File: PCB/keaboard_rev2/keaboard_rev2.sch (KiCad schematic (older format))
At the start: 78 parts, among them J1 AudioJack4, SW1 SW_Push, SW10 SW_Push, SW11 SW_Push, SW12 SW_Push, SW13 SW_Push, SW14 SW_Push, SW15 SW_Push, SW16 SW_Push, SW17 SW_Push, SW18 SW_Push, SW19 SW_Push, SW2 SW_Push, SW20 SW_Push, SW21 SW_Push, SW22 SW_Push, SW23 SW_Push, SW24 SW_Push, SW25 SW_Push, SW3 SW_Push, SW4 SW_Push, SW5 SW_Push, SW6 SW_Push, SW7 SW_Push, SW8 SW_Push, SW9 SW_Push, U1 ProMicro

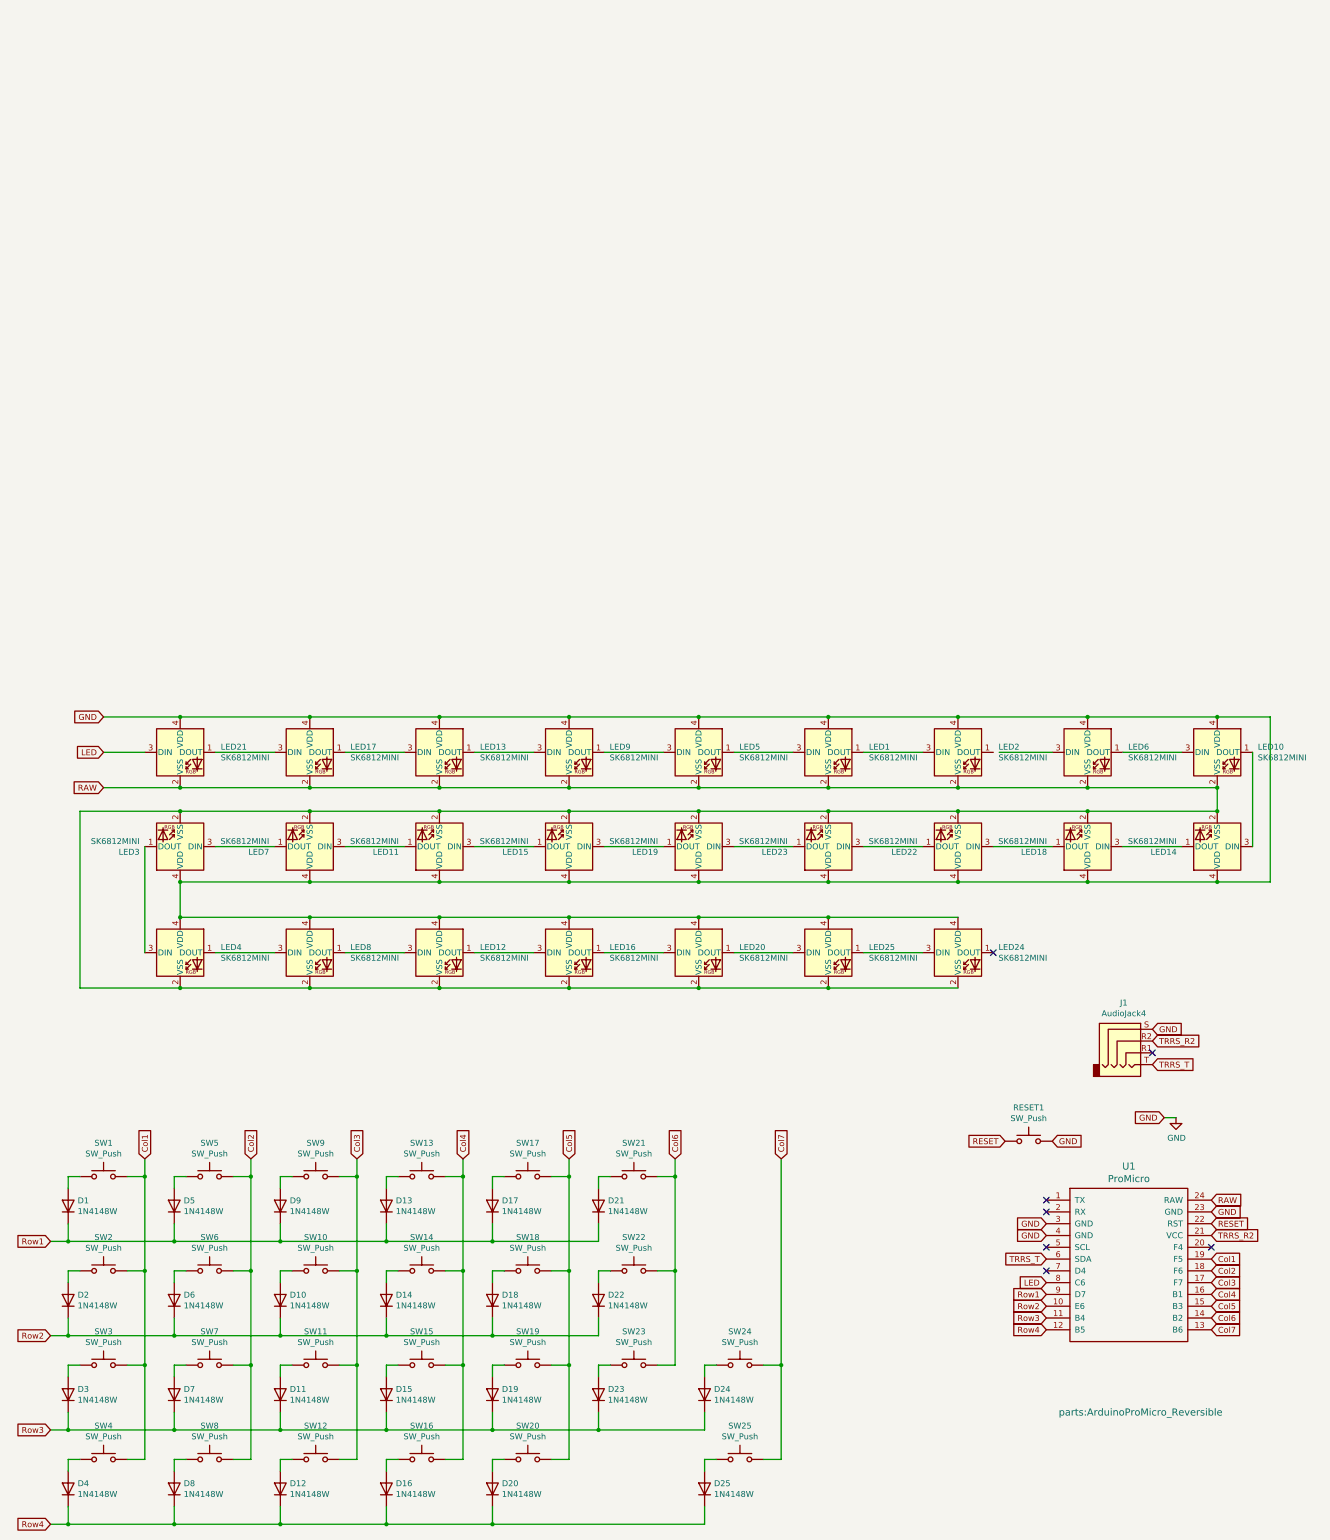
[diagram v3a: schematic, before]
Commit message: Better footprints, OLED, misc
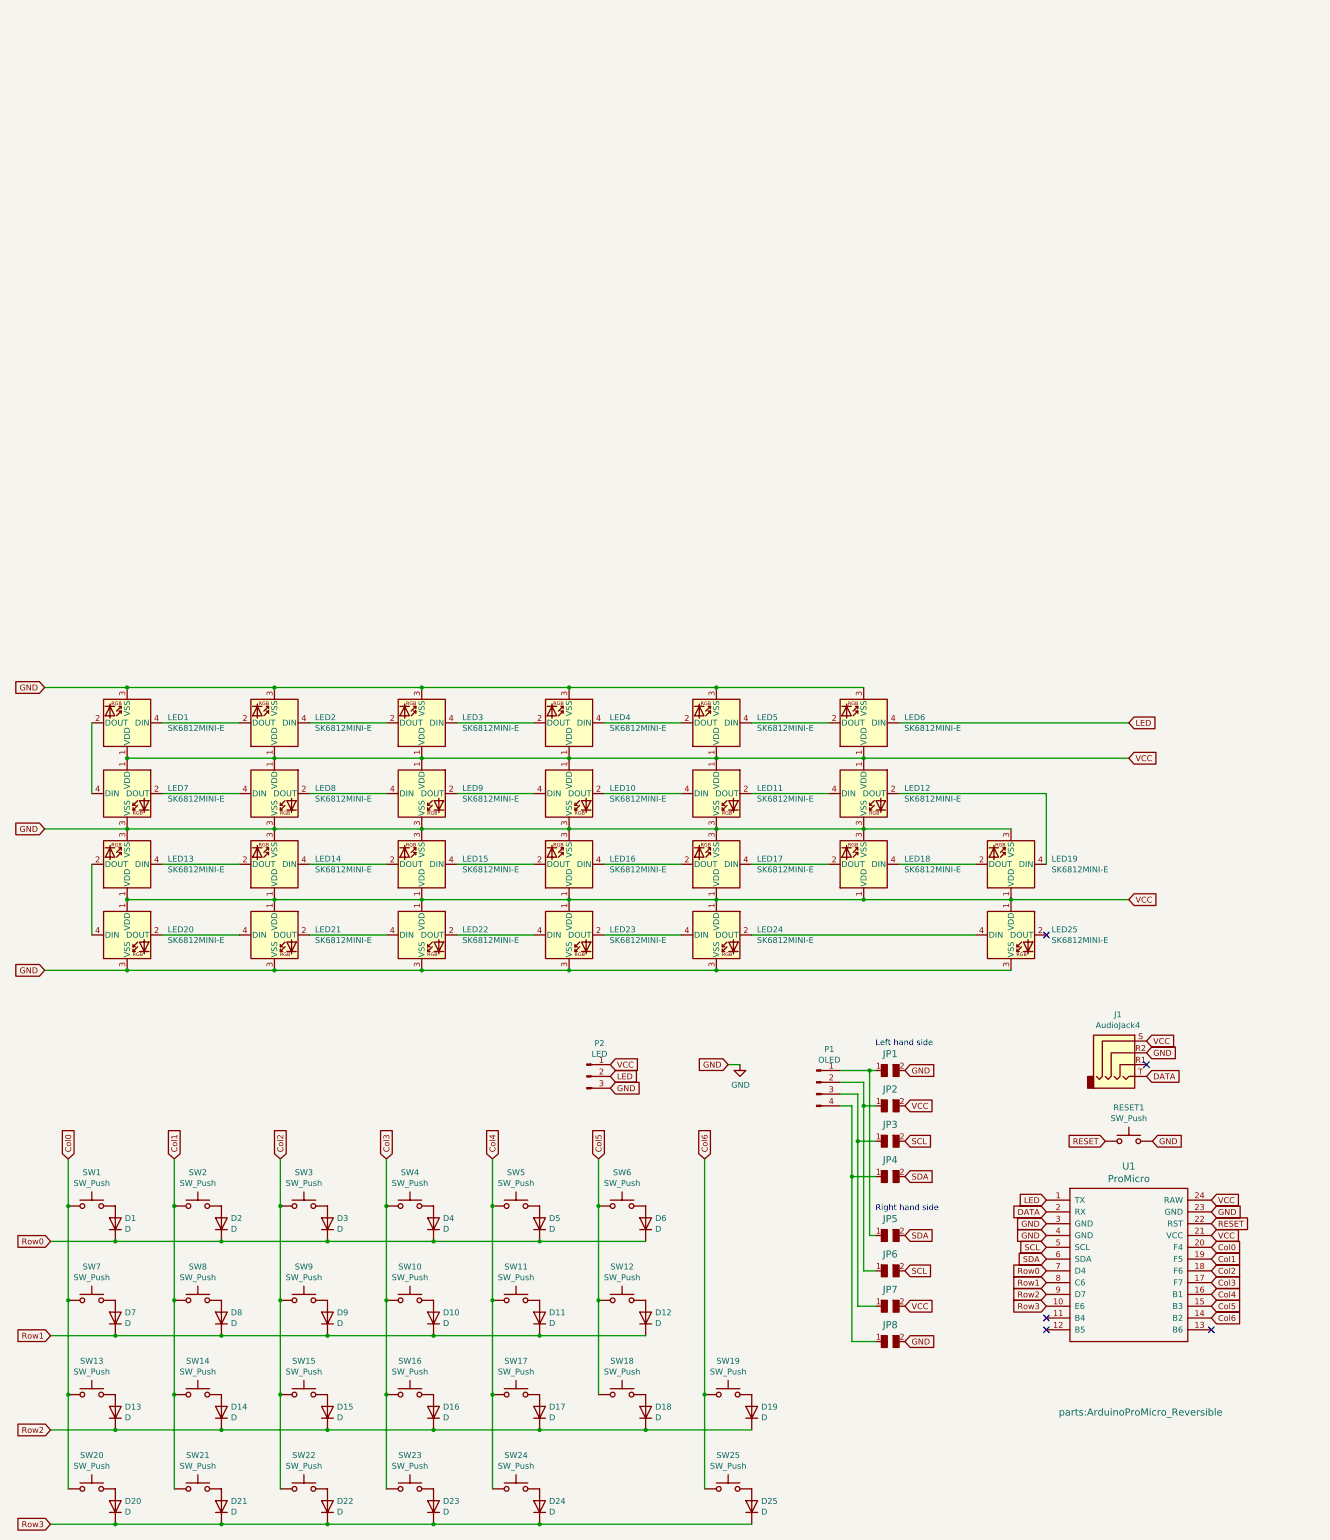
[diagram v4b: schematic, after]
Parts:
- removed LED1, LED10, LED11, LED12, LED13, LED14, LED15, LED16, LED17, LED18, LED19, LED2, LED20, LED21, LED22, LED23, LED24, LED25, LED3, LED4, LED5, LED6, LED7, LED8, LED9: SK6812MINI, parts:YS-SK6812MINI-E_reversible, symbol LED:SK6812MINI
- added JP1, JP8: GND, kbd:Jumper, symbol keyboard_parts:SOLDER_JUMPER
- added JP2, JP7: VCC, kbd:Jumper, symbol keyboard_parts:SOLDER_JUMPER
- added JP3, JP6: SCL, kbd:Jumper, symbol keyboard_parts:SOLDER_JUMPER
- added JP4, JP5: SDA, kbd:Jumper, symbol keyboard_parts:SOLDER_JUMPER
- added LED1, LED10, LED11, LED12, LED13, LED14, LED15, LED16, LED17, LED18, LED19, LED2, LED20, LED21, LED22, LED23, LED24, LED25, LED3, LED4, LED5, LED6, LED7, LED8, LED9: SK6812MINI-E, parts:SK6812MINI-E_reversible, symbol kicad-keyboard-parts:SK6812MINI-E
- added P1: OLED, kbd:OLED_v2, symbol Connector:Conn_01x04_Male
- added P2: LED, parts:StripLED_reversible, symbol Connector:Conn_01x03_Male
- D1, D10, D11, D12, D13, D14, D15, D16, D17, D18, D19, D2, D20, D21, D22, D23, D24, D25, D3, D4, D5, D6, D7, D8, D9: value 1N4148W -> D; footprint parts:D_SOD123_reversible -> Keebio-Parts:Diode-dual
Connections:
- net Col1: now also SW14.1, SW2.1, SW21.1, SW8.1; no longer SW1.2, SW2.2, SW3.2, SW4.2
- net Col2: now also SW15.1, SW22.1, SW3.1, SW9.1; no longer SW5.2, SW6.2, SW7.2, SW8.2
- net Col3: now also SW10.1, SW16.1, SW23.1, SW4.1; no longer SW10.2, SW11.2, SW12.2, SW9.2
- net Col4: now also SW11.1, SW17.1, SW24.1, SW5.1; no longer SW13.2, SW14.2, SW15.2, SW16.2
- net Col5: now also SW12.1, SW18.1, SW6.1; no longer SW17.2, SW18.2, SW19.2, SW20.2
- net Col6: now also SW19.1, SW25.1; no longer SW21.2, SW22.2, SW23.2
- net GND: now also J1.R2, JP1.2, JP8.2, LED1.3 (VSS), LED10.3 (VSS), LED11.3 (VSS), LED12.3 (VSS), LED13.3 (VSS), LED14.3 (VSS), LED15.3 (VSS), LED16.3 (VSS), LED17.3 (VSS), LED18.3 (VSS), LED19.3 (VSS), LED2.3 (VSS), LED20.3 (VSS), LED21.3 (VSS), LED22.3 (VSS), LED23.3 (VSS), LED24.3 (VSS), LED25.3 (VSS), LED3.3 (VSS), LED4.3 (VSS), LED5.3 (VSS), LED6.3 (VSS), LED7.3 (VSS), LED8.3 (VSS), LED9.3 (VSS), P2.3 (Pin_3); no longer J1.S
- net LED: now also U1.1 (TX), LED6.4 (DIN), P2.2 (Pin_2); no longer U1.8 (C6)
- net Row1: now also D10.1 (K), D11.1 (K), D12.1 (K), D7.1 (K), D8.1 (K), U1.8 (C6); no longer D1.1 (K), D13.1 (K), D17.1 (K), D21.1 (K), D5.1 (K), U1.9 (D7)
- net Row2: now also D13.1 (K), D15.1 (K), D16.1 (K), D17.1 (K), D19.1 (K), U1.9 (D7); no longer D10.1 (K), D2.1 (K), D22.1 (K), D6.1 (K), U1.10 (E6)
- net Row3: now also D20.1 (K), D21.1 (K), D22.1 (K), D25.1 (K), U1.10 (E6); no longer D11.1 (K), D15.1 (K), D19.1 (K), D3.1 (K), D7.1 (K), U1.11 (B4)
- net DATA: now reaches U1.2 (RX)
- net DATA: now also J1.T
- net Col0: now reaches U1.20 (F4)
- net Col0: now also SW1.1, SW13.1, SW20.1, SW7.1
- net SCL: now reaches U1.5 (SCL)
- net SCL: now also JP3.2, JP6.2
- net Row0: now reaches U1.7 (D4)
- net Row0: now also D1.1 (K), D2.1 (K), D3.1 (K), D4.1 (K), D5.1 (K), D6.1 (K)
- net at D1.2 (A): now also SW1.2; no longer SW1.1
- net at D5.2 (A): now also SW5.2; no longer SW5.1
- net at D9.2 (A): now also SW9.2; no longer SW9.1
- net at D13.2 (A): now also SW13.2; no longer SW13.1
- net at D17.2 (A): now also SW17.2; no longer SW17.1
- net at D21.2 (A): now also SW21.2; no longer SW21.1
- net at D22.2 (A): now also SW22.2; no longer SW22.1
- net at D18.2 (A): now also SW18.2; no longer SW18.1
- net at D14.2 (A): now also SW14.2; no longer SW14.1
- net at D10.2 (A): now also SW10.2; no longer SW10.1
- net at D6.2 (A): now also SW6.2; no longer SW6.1
- net at D2.2 (A): now also SW2.2; no longer SW2.1
- net at D3.2 (A): now also SW3.2; no longer SW3.1
- net at D7.2 (A): now also SW7.2; no longer SW7.1
- net at D11.2 (A): now also SW11.2; no longer SW11.1
- net at D15.2 (A): now also SW15.2; no longer SW15.1
- net at D19.2 (A): now also SW19.2; no longer SW19.1
- net at D23.2 (A): now also SW23.2; no longer SW23.1
- net at D24.2 (A): now also SW24.2; no longer SW24.1
- net at D25.2 (A): now also SW25.2; no longer SW25.1
- net at D20.2 (A): now also SW20.2; no longer SW20.1
- net at D16.2 (A): now also SW16.2; no longer SW16.1
- net at D12.2 (A): now also SW12.2; no longer SW12.1
- net at D8.2 (A): now also SW8.2; no longer SW8.1
- net at D4.2 (A): now also SW4.2; no longer SW4.1
- removed net Col7: SW24.2, SW25.2, U1.13 (B6)
- net RAW renamed VCC
- net VCC: now also J1.S, U1.21 (VCC), JP2.2, JP7.2, LED1.1 (VDD), LED10.1 (VDD), LED11.1 (VDD), LED12.1 (VDD), LED13.1 (VDD), LED14.1 (VDD), LED15.1 (VDD), LED16.1 (VDD), LED17.1 (VDD), LED18.1 (VDD), LED19.1 (VDD), LED2.1 (VDD), LED20.1 (VDD), LED21.1 (VDD), LED22.1 (VDD), LED23.1 (VDD), LED24.1 (VDD), LED25.1 (VDD), LED3.1 (VDD), LED4.1 (VDD), LED5.1 (VDD), LED6.1 (VDD), LED7.1 (VDD), LED8.1 (VDD), LED9.1 (VDD), P2.1 (Pin_1)
- removed net Row4: D12.1 (K), D16.1 (K), D20.1 (K), D25.1 (K), D4.1 (K), D8.1 (K), U1.12 (B5)
- removed net TRRS_R2: J1.R2, U1.21 (VCC)
- net TRRS_T renamed SDA
- net SDA: now also JP4.2, JP5.2; no longer J1.T
- new net: JP1.1, JP5.1, P1.1 (Pin_1)
- new net: JP2.1, JP6.1, P1.2 (Pin_2)
- new net: JP3.1, JP7.1, P1.3 (Pin_3)
- new net: JP4.1, JP8.1, P1.4 (Pin_4)
- new net: LED5.4 (DIN), LED6.2 (DOUT)
- new net: LED4.4 (DIN), LED5.2 (DOUT)
- new net: LED3.4 (DIN), LED4.2 (DOUT)
- new net: LED2.4 (DIN), LED3.2 (DOUT)
- new net: LED1.4 (DIN), LED2.2 (DOUT)
- new net: LED1.2 (DOUT), LED7.4 (DIN)
- new net: LED7.2 (DOUT), LED8.4 (DIN)
- new net: LED8.2 (DOUT), LED9.4 (DIN)
- new net: LED10.4 (DIN), LED9.2 (DOUT)
- new net: LED10.2 (DOUT), LED11.4 (DIN)
- new net: LED11.2 (DOUT), LED12.4 (DIN)
- new net: LED12.2 (DOUT), LED19.4 (DIN)
- new net: LED17.4 (DIN), LED18.2 (DOUT)
- new net: LED18.4 (DIN), LED19.2 (DOUT)
- new net: LED16.4 (DIN), LED17.2 (DOUT)
- new net: LED15.4 (DIN), LED16.2 (DOUT)
- new net: LED14.4 (DIN), LED15.2 (DOUT)
- new net: LED13.4 (DIN), LED14.2 (DOUT)
- new net: LED13.2 (DOUT), LED20.4 (DIN)
- new net: LED20.2 (DOUT), LED21.4 (DIN)
- new net: LED21.2 (DOUT), LED22.4 (DIN)
- new net: LED22.2 (DOUT), LED23.4 (DIN)
- new net: LED23.2 (DOUT), LED24.4 (DIN)
- new net: LED24.2 (DOUT), LED25.4 (DIN)
- no-connect marks 7 -> 5
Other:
- note added: "Left hand side"
- note added: "Right hand side"
- moved on the sheet: D1, J1, RESET1, SW1

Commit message: WIP
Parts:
- removed LED19: SK6812MINI-E, parts:SK6812MINI-E_reversible, symbol kicad-keyboard-parts:SK6812MINI-E
- added D13, D14, D15, D16, D17, D18: D, Keebio-Parts:Diode-dual, symbol Diode:1N4148W
- added LED25, LED26, LED27, LED28, LED29, LED30, LED31: SK6812MINI-E, parts:SK6812MINI-E_reversible, symbol kicad-keyboard-parts:SK6812MINI-E
- added SW13, SW14, SW15, SW16, SW17, SW18: SW_Push, keyswitches:Kailh_socket_PG1350_reversible, symbol Switch:SW_Push
- renumbered D13 to D19, D14 to D20, D15 to D21, D16 to D22, D17 to D23, D18 to D24, D19 to D25, D20 to D26, D21 to D27, D22 to D28, D23 to D29, D24 to D30, D25 to D31, LED20 to LED19, LED21 to LED20, LED22 to LED21, LED23 to LED22, LED24 to LED23, LED25 to LED24, SW13 to SW19, SW14 to SW20, SW15 to SW21, SW16 to SW22, SW17 to SW23, SW18 to SW24, SW19 to SW25, SW20 to SW26, SW21 to SW27, SW22 to SW28, SW23 to SW29, SW24 to SW30, SW25 to SW31
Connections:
- net Col0: now also SW13.1
- net Col1: now also SW14.1
- net Col2: now also SW15.1
- net Col3: now also SW16.1
- net Col4: now also SW17.1
- net Col5: now also SW18.1
- net GND: now also LED25.3 (VSS), LED26.3 (VSS), LED27.3 (VSS), LED28.3 (VSS), LED29.3 (VSS), LED30.3 (VSS), LED31.3 (VSS)
- net Row2: now also D13.1 (K), D14.1 (K), D15.1 (K), D16.1 (K), D17.1 (K), D18.1 (K); no longer D19.1 (K), D20.1 (K), D21.1 (K), D22.1 (K), D23.1 (K), D24.1 (K), D25.1 (K)
- net Row3: now also D19.1 (K), D20.1 (K), D21.1 (K), D22.1 (K), D23.1 (K), D24.1 (K), D25.1 (K); no longer D26.1 (K), D27.1 (K), D28.1 (K), D29.1 (K), D30.1 (K), D31.1 (K)
- net VCC: now also LED25.1 (VDD), LED26.1 (VDD), LED27.1 (VDD), LED28.1 (VDD), LED29.1 (VDD), LED30.1 (VDD), LED31.1 (VDD)
- net Row4: now reaches U1.11 (B4)
- net Row4: now also D26.1 (K), D27.1 (K), D28.1 (K), D29.1 (K), D30.1 (K), D31.1 (K)
- net at LED12.2 (DOUT): now also LED18.4 (DIN)
- net at LED24.2 (DOUT): now also LED25.4 (DIN)
- new net: D18.2 (A), SW18.2
- new net: D17.2 (A), SW17.2
- new net: D16.2 (A), SW16.2
- new net: D15.2 (A), SW15.2
- new net: D14.2 (A), SW14.2
- new net: D13.2 (A), SW13.2
- new net: LED25.2 (DOUT), LED31.4 (DIN)
- new net: LED26.4 (DIN), LED27.2 (DOUT)
- new net: LED27.4 (DIN), LED28.2 (DOUT)
- new net: LED28.4 (DIN), LED29.2 (DOUT)
- new net: LED29.4 (DIN), LED30.2 (DOUT)
- new net: LED30.4 (DIN), LED31.2 (DOUT)
- no-connect marks 5 -> 4
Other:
- moved on the sheet: D1, D10, D11, D12, D19, D2, D20, D21, D22, D23, D24, D25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
